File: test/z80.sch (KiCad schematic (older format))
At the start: 22 parts

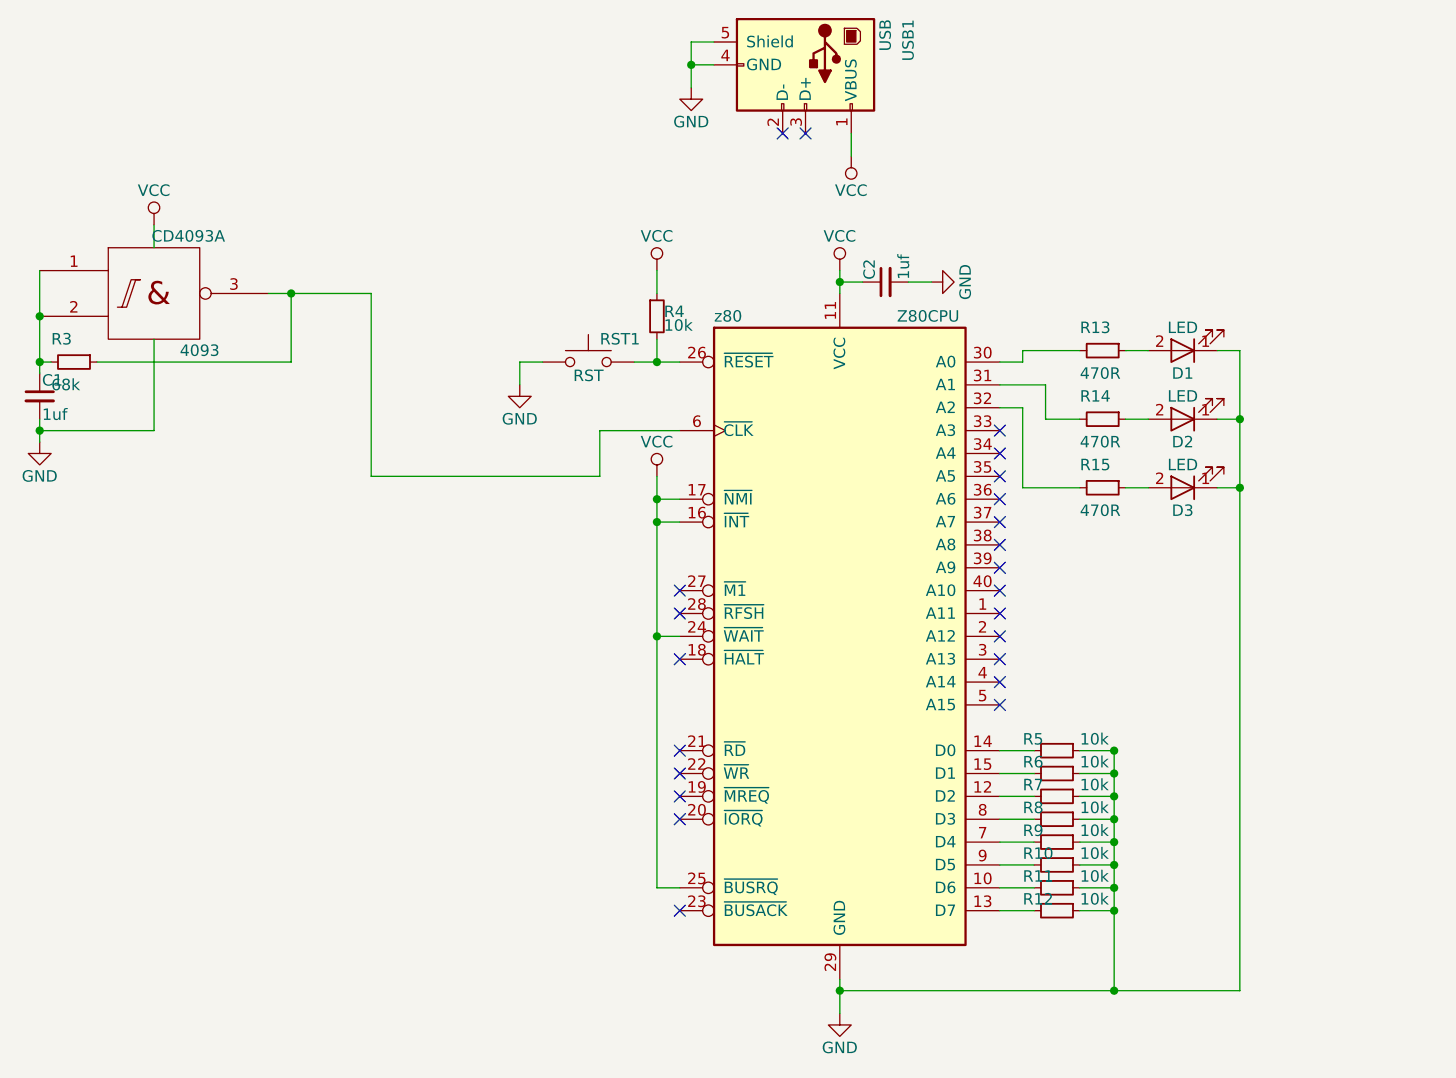
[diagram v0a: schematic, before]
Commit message: Test board revision 2
- Replaced quad NAND gate with single NOT gate
- Broke out remaining address lines to LEDs
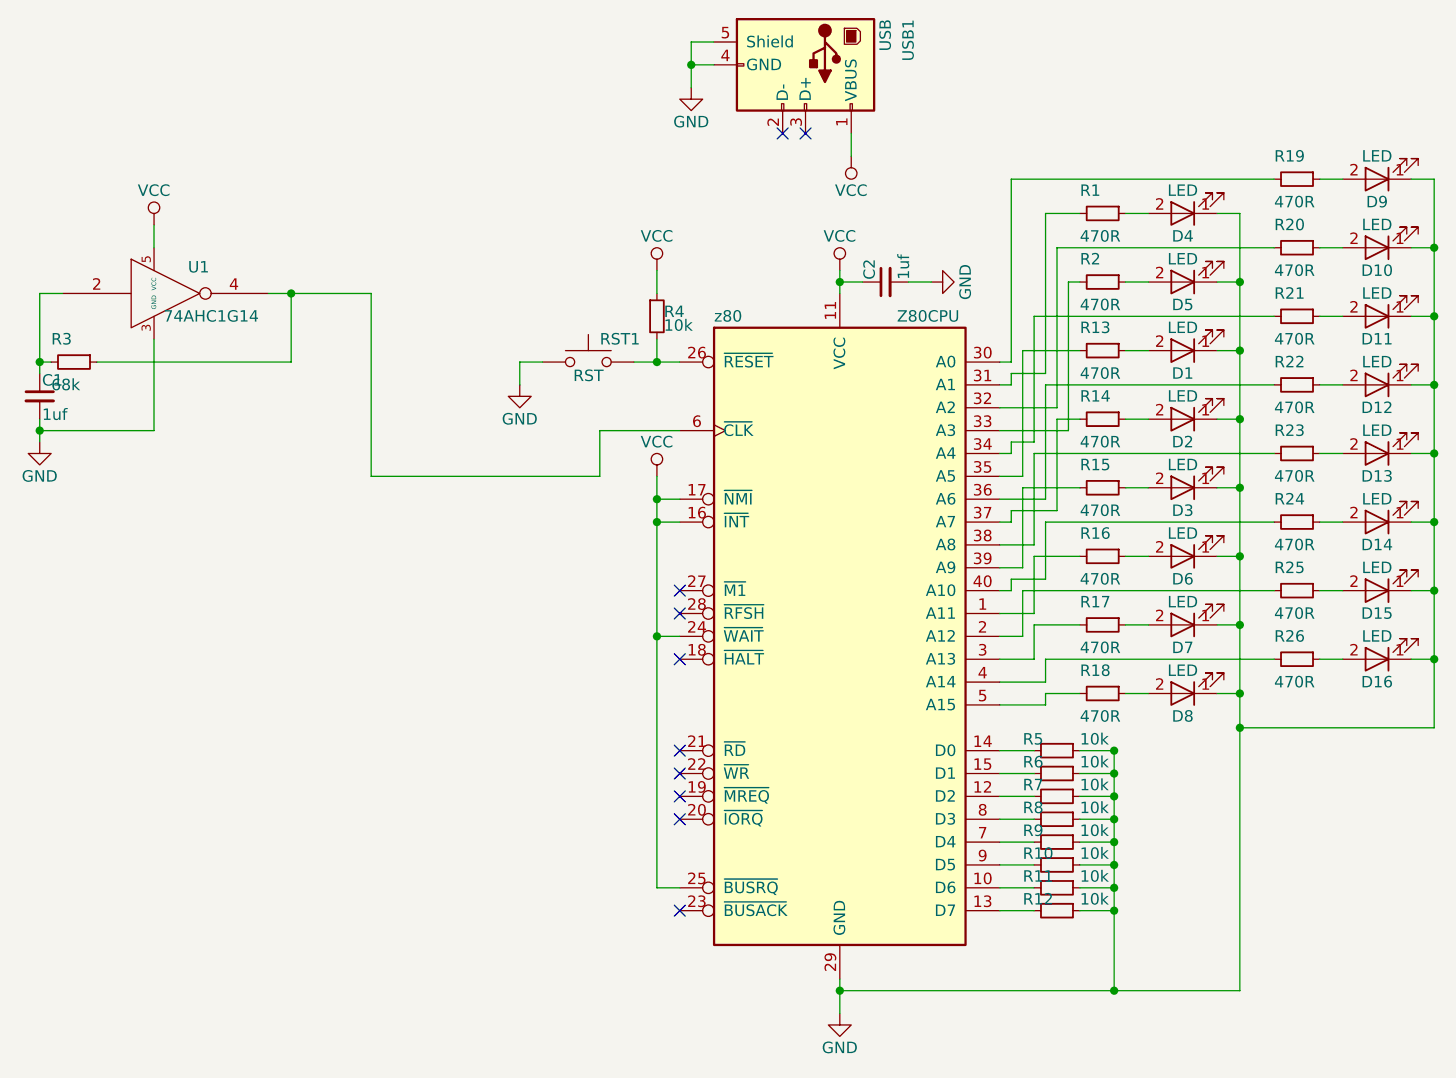
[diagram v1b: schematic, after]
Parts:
- removed CD4093: 4093, SMD_Packages:SOIC-14_N, symbol 4093
- added D10, D11, D12, D13, D14, D15, D16, D4, D5, D6, D7, D8, D9: LED, LEDs:LED_0805, symbol LED
- added R1, R16, R17, R18, R19, R2, R20, R21, R22, R23, R24, R25, R26: 470R, Resistors_SMD:R_0805_HandSoldering, symbol R_Small
- added U1: 74AHC1G14, TO_SOT_Packages_SMD:SOT-353_SC-70-5_Handsoldering, symbol 74AHC1G14
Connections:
- net GND: now also D10.1 (K), D11.1 (K), D12.1 (K), D13.1 (K), D14.1 (K), D15.1 (K), D16.1 (K), D4.1 (K), D5.1 (K), D6.1 (K), D7.1 (K), D8.1 (K), D9.1 (K), U1.3 (GND)
- net VCC: now also U1.5 (VCC)
- net at z80.1 (A11): now also R16.2
- net at z80.2 (A12): now also R25.2
- net at z80.3 (A13): now also R17.2
- net at z80.30 (A0): now also R19.2; no longer R13.2
- net at z80.31 (A1): now also R1.2; no longer R14.2
- net at z80.32 (A2): now also R20.2; no longer R15.2
- net at z80.33 (A3): now also R2.2
- net at z80.34 (A4): now also R21.2
- net at z80.35 (A5): now also R13.2
- net at z80.36 (A6): now also R22.2
- net at z80.37 (A7): now also R14.2
- net at z80.38 (A8): now also R23.2
- net at z80.39 (A9): now also R15.2
- net at z80.4 (A14): now also R26.2
- net at z80.40 (A10): now also R24.2
- net at z80.5 (A15): now also R18.2
- net at R3.1, z80.6 (~CLK~): now also U1.4
- net at C1.1, R3.2: now also U1.2
- new net: D6.2 (A), R16.1
- new net: D7.2 (A), R17.1
- new net: D8.2 (A), R18.1
- new net: D4.2 (A), R1.1
- new net: D5.2 (A), R2.1
- new net: D11.2 (A), R21.1
- new net: D12.2 (A), R22.1
- new net: D13.2 (A), R23.1
- new net: D14.2 (A), R24.1
- new net: D15.2 (A), R25.1
- new net: D16.2 (A), R26.1
- new net: D9.2 (A), R19.1
- new net: D10.2 (A), R20.1
- no-connect marks 23 -> 10
